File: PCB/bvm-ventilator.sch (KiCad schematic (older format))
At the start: 1 part, among them U13 IEC_CONNECTOR

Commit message: Checkpoint
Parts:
- added TP?: TestPoint, symbol Connector:TestPoint
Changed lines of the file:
@@
 $EndSheet
 $Sheet
-S 7200 4850 550  200
+S 6800 4850 550  200
 U 5E8EB699
 F0 "Alarm buzzer" 50
 F1 "BUZZER.sch" 50
-F2 "ENABLE" I R 7750 4950 50
-$EndSheet
-$Sheet
-S 7200 5300 550  600
+F2 "ENABLE" I R 7350 4950 50
+$EndSheet
+$Sheet
+S 6800 5300 550  600
 U 5E8F3A13
 F0 "OLED" 50
 F1 "SSD1306_OLED.sch" 50
-F2 "SCL" I R 7750 5500 50
-F3 "SDA" I R 7750 5400 50
-F4 "MOSI" I L 7200 5400 50
-F5 "SCK" I L 7200 5500 50
-F6 "DC" I L 7200 5700 50
-F7 "CS" I L 7200 5800 50
-F8 "RES" I L 7200 5600 50
+F2 "SCL" I R 7350 5500 50
+F3 "SDA" I R 7350 5400 50
+F4 "MOSI" I L 6800 5400 50
+F5 "SCK" I L 6800 5500 50
+F6 "DC" I L 6800 5700 50
+F7 "CS" I L 6800 5800 50
+F8 "RES" I L 6800 5600 50
 $EndSheet
 $Sheet
@@
 Text Label 6450 3900 2    50   ~ 0
 SCL
-Text Label 7750 5400 0    50   ~ 0
-SDA
-Text Label 7750 5500 0    50   ~ 0
+Text Label 7350 5400 0    50   ~ 0
+SDA
+Text Label 7350 5500 0    50   ~ 0
 SCL
 Text Label 3400 2800 0    50   ~ 0
@@
 Text Label 7300 3950 0    50   ~ 0
 STEPPER_DIR
-Text Label 7750 4950 0    50   ~ 0
+Text Label 7350 4950 0    50   ~ 0
 BUZZ_ENABLE
 Text Label 6450 3150 2    50   ~ 0
@@
 VBATT_SENSE
 $Sheet
-S 5450 4850 550  400
+S 5050 4850 550  400
 U 5E8BEE14
 F0 "Rotarty Encoder" 50
 F1 "ROTARY_ENCODER.sch" 50
-F2 "A" O R 6000 4950 50
-F3 "B" O R 6000 5050 50
-F4 "BUTTON" O R 6000 5150 50
-$EndSheet
-Text Label 6000 4950 0    50   ~ 0
+F2 "A" O R 5600 4950 50
+F3 "B" O R 5600 5050 50
+F4 "BUTTON" O R 5600 5150 50
+$EndSheet
+Text Label 5600 4950 0    50   ~ 0
 ROTARY_ENCODER_A
-Text Label 6000 5050 0    50   ~ 0
+Text Label 5600 5050 0    50   ~ 0
 ROTARY_ENCODER_B
-Text Label 6000 5150 0    50   ~ 0
+Text Label 5600 5150 0    50   ~ 0
 ROTARY_ENCODER_BUTTON
 Text Label 7300 3350 0    50   ~ 0
@@
 ROTARY_ENCODER_BUTTON
 $Sheet
-S 5450 5500 550  200
+S 5050 5500 550  200
 U 5E8CBD7F
 F0 "BUTTON_1" 50
 F1 "BUTTON.sch" 50
-F2 "OUT" O R 6000 5600 50
-$EndSheet
-Text Label 6000 5600 0    50   ~ 0
+F2 "OUT" O R 5600 5600 50
+$EndSheet
+Text Label 5600 5600 0    50   ~ 0
 BUTTON_1
 Text Label 6450 3450 2    50   ~ 0
@@
 Text Label 6450 3550 2    50   ~ 0
 DISPLAY_DC
-Text Label 7200 5700 2    50   ~ 0
+Text Label 6800 5700 2    50   ~ 0
 DISPLAY_DC
-Text Label 7200 5800 2    50   ~ 0
+Text Label 6800 5800 2    50   ~ 0
 DISPLAY_CS
-Text Label 7200 5600 2    50   ~ 0
+Text Label 6800 5600 2    50   ~ 0
 MISO
-Text Label 7200 5400 2    50   ~ 0
+Text Label 6800 5400 2    50   ~ 0
 MOSI
-Text Label 7200 5500 2    50   ~ 0
+Text Label 6800 5500 2    50   ~ 0
 SCK
 Wire Notes Line
 	4950 4700 4950 6050
 Wire Notes Line
-	4950 6050 8350 6050
-Wire Notes Line
-	8350 6050 8350 4700
-Wire Notes Line
-	8350 4700 4950 4700
+	4950 6050 7900 6050
+Wire Notes Line
+	7900 6050 7900 4700
+Wire Notes Line
+	7900 4700 4950 4700
 Text Notes 2750 3850 0    79   ~ 0
 Motion Control
@@
 Text Notes 4550 2950 0    79   ~ 0
 Misc.
+$Comp
+L Connector:TestPoint TP?
+U 1 1 5E8ED4B0
+P 8500 5000
+F 0 "TP?" H 8558 5118 50  0000 L CNN
+F 1 "TestPoint" H 8558 5027 50  0000 L CNN
+F 2 "" H 8700 5000 50  0001 C CNN
+F 3 "~" H 8700 5000 50  0001 C CNN
+	1    8500 5000
+	1    0    0    -1
+$EndComp
 $EndSCHEMATC

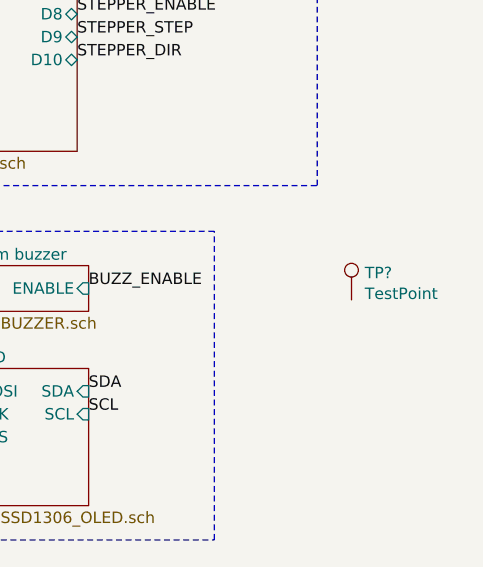
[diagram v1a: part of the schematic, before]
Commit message: Moved submodules into PCB subdirectory
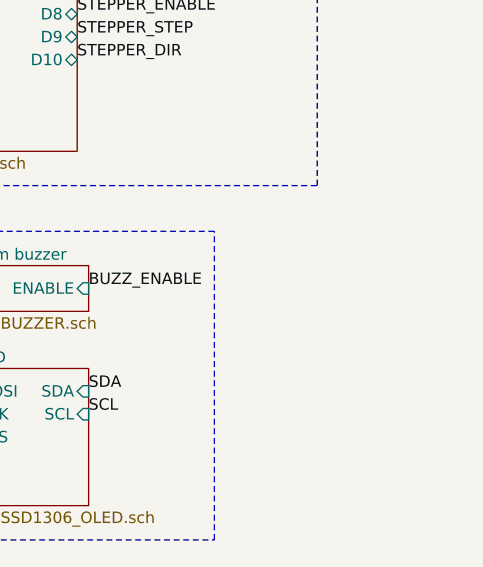
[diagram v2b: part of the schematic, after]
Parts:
- removed TP?: TestPoint, symbol Connector:TestPoint
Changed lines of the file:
@@
 Text Notes 4550 2950 0    79   ~ 0
 Misc.
-$Comp
-L Connector:TestPoint TP?
-U 1 1 5E8ED4B0
-P 8500 5000
-F 0 "TP?" H 8558 5118 50  0000 L CNN
-F 1 "TestPoint" H 8558 5027 50  0000 L CNN
-F 2 "" H 8700 5000 50  0001 C CNN
-F 3 "~" H 8700 5000 50  0001 C CNN
-	1    8500 5000
-	1    0    0    -1
-$EndComp
 $EndSCHEMATC

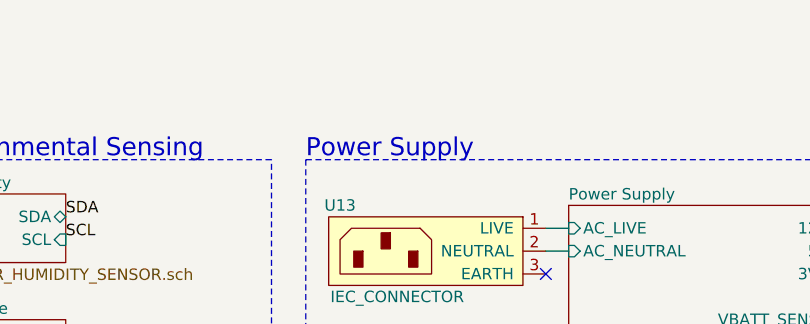
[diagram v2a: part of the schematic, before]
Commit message: Added test points to sensors
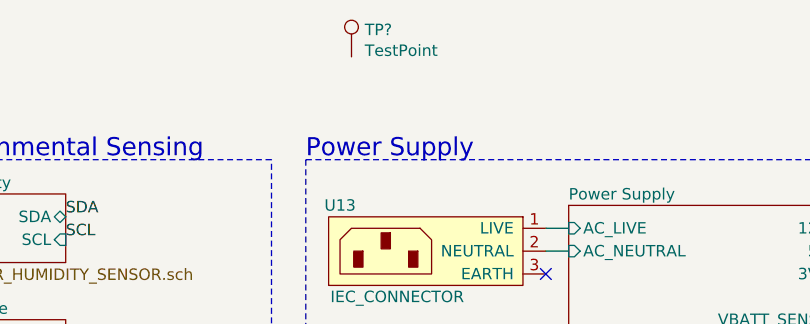
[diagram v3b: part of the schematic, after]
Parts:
- added TP?: TestPoint, symbol Connector:TestPoint
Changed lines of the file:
@@
 Text Notes 4550 2950 0    79   ~ 0
 Misc.
+$Comp
+L Connector:TestPoint TP?
+U 1 1 5E923993
+P 4650 1300
+F 0 "TP?" H 4708 1418 50  0000 L CNN
+F 1 "TestPoint" H 4708 1327 50  0000 L CNN
+F 2 "" H 4850 1300 50  0001 C CNN
+F 3 "~" H 4850 1300 50  0001 C CNN
+	1    4650 1300
+	1    0    0    -1
+$EndComp
 $EndSCHEMATC

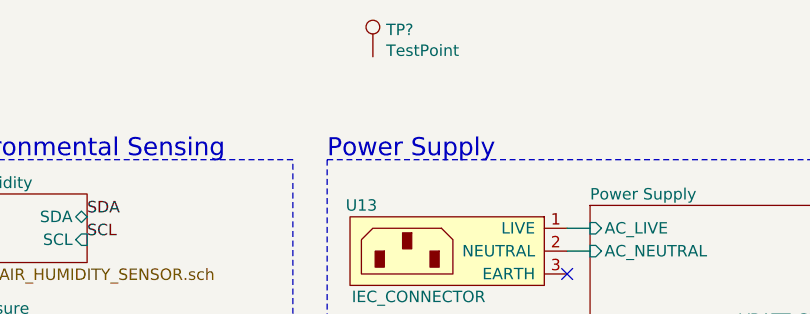
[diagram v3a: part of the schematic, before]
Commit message: Added correct DRV breakout and added testpoints
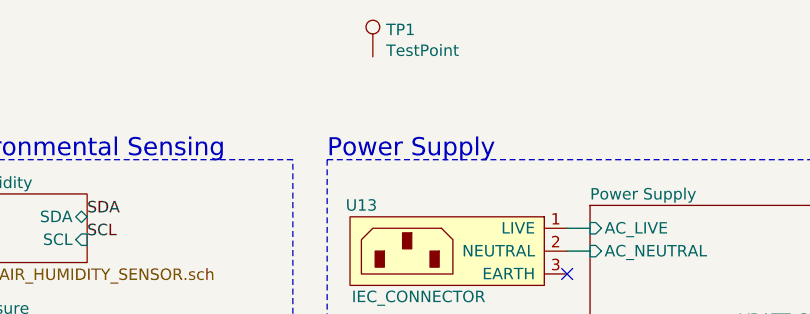
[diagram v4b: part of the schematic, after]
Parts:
- gave numbers to parts that had none: 1
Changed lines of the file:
@@
 Misc.
 $Comp
-L Connector:TestPoint TP?
+L Connector:TestPoint TP1
 U 1 1 5E923993
 P 4650 1300
-F 0 "TP?" H 4708 1418 50  0000 L CNN
+F 0 "TP1" H 4708 1418 50  0000 L CNN
 F 1 "TestPoint" H 4708 1327 50  0000 L CNN
 F 2 "" H 4850 1300 50  0001 C CNN

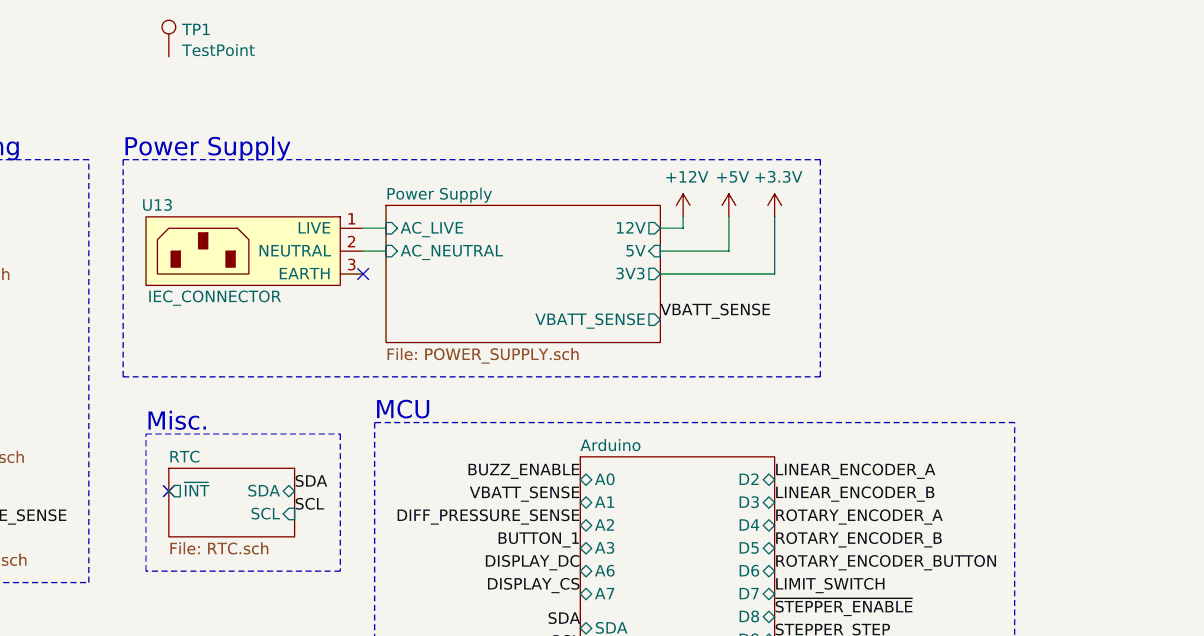
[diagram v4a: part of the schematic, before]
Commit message: Added test points to PSU
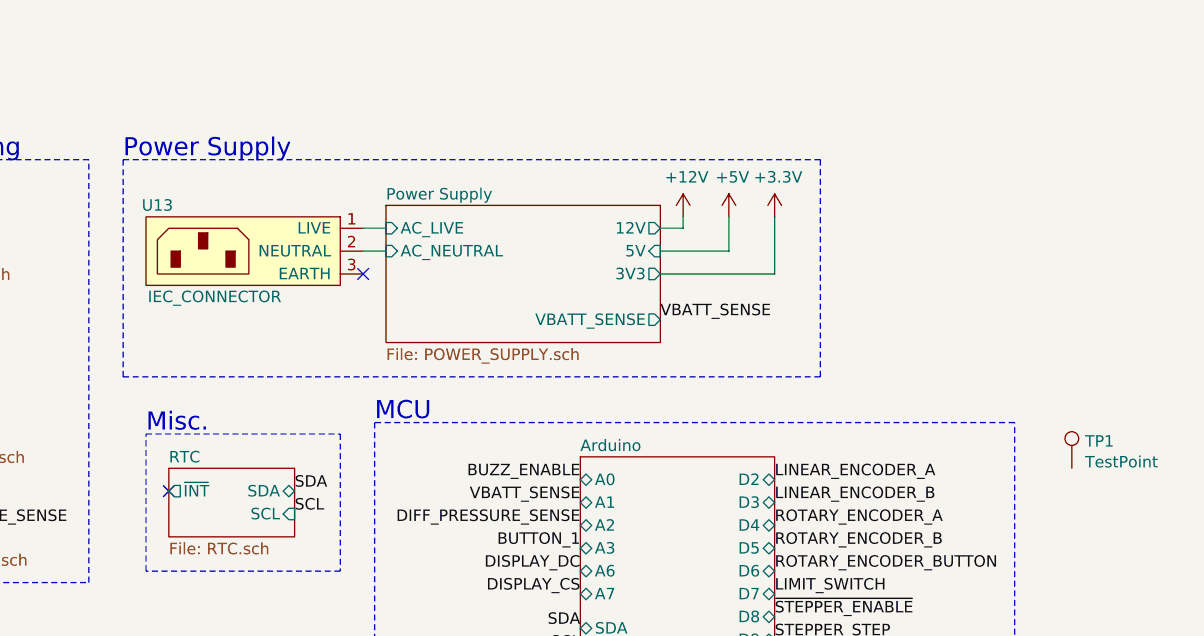
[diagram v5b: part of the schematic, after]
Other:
- moved on the sheet: TP1
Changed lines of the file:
@@
 L Connector:TestPoint TP1
 U 1 1 5E923993
-P 4650 1300
-F 0 "TP1" H 4708 1418 50  0000 L CNN
-F 1 "TestPoint" H 4708 1327 50  0000 L CNN
-F 2 "" H 4850 1300 50  0001 C CNN
-F 3 "~" H 4850 1300 50  0001 C CNN
-	1    4650 1300
+P 8600 3100
+F 0 "TP1" H 8658 3218 50  0000 L CNN
+F 1 "TestPoint" H 8658 3127 50  0000 L CNN
+F 2 "" H 8800 3100 50  0001 C CNN
+F 3 "~" H 8800 3100 50  0001 C CNN
+	1    8600 3100
 	1    0    0    -1
 $EndComp

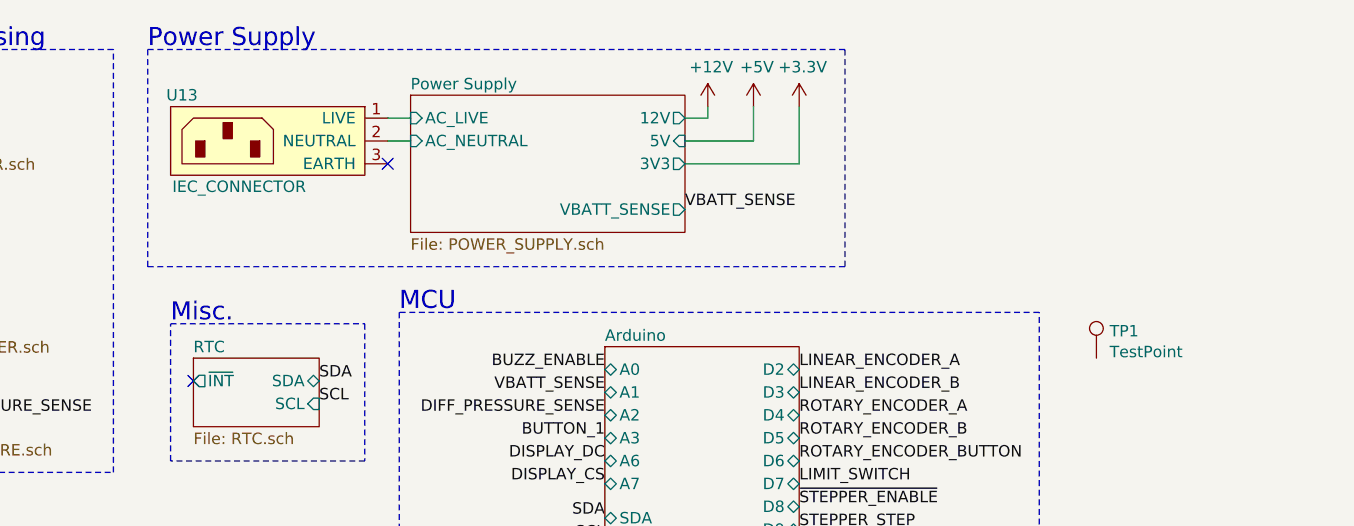
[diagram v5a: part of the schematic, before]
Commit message: Added remaining test points
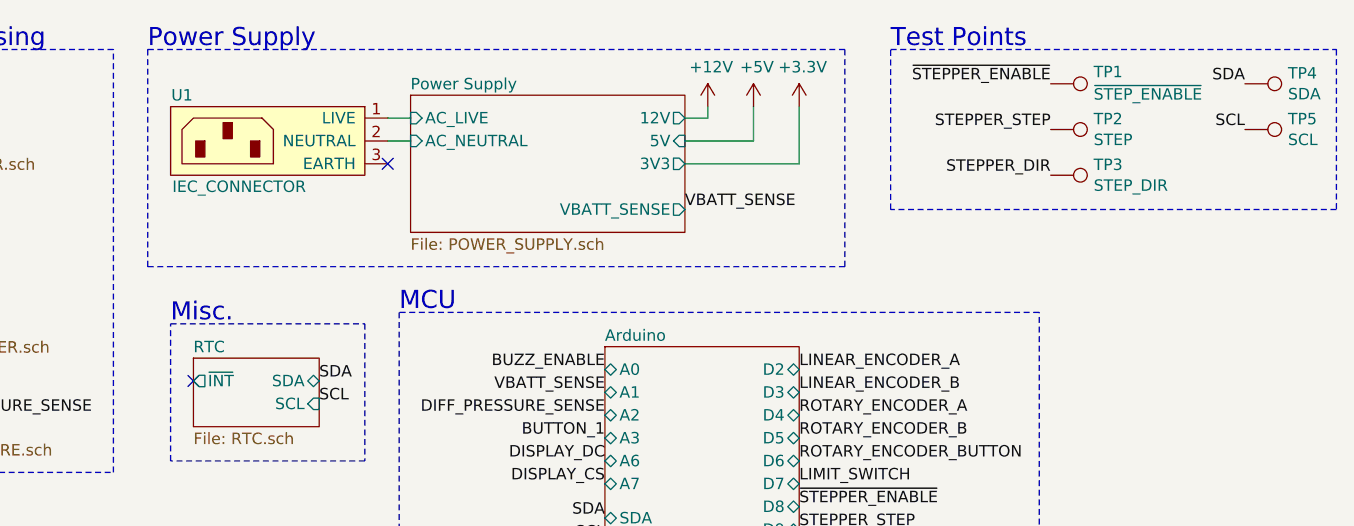
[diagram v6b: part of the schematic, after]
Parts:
- added TP2: STEP, symbol Connector:TestPoint
- added TP3: STEP_DIR, symbol Connector:TestPoint
- added TP4: SDA, symbol Connector:TestPoint
- added TP5: SCL, symbol Connector:TestPoint
- TP1: value TestPoint -> ~STEP_ENABLE
- renumbered U13 to U1
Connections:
- net SCL: now also TP5.1
- net SDA: now also TP4.1
- net STEPPER_DIR: now also TP3.1
- net STEPPER_STEP: now also TP2.1
- net ~STEPPER_ENABLE: now also TP1.1
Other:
- note added: "Test Points"
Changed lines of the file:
@@
 VBATT_SENSE
 $Comp
-L power:+3.3V #PWR04
+L power:+3.3V #PWR05
 U 1 1 5E8B3135
 P 7300 2000
-F 0 "#PWR04" H 7300 1850 50  0001 C CNN
+F 0 "#PWR05" H 7300 1850 50  0001 C CNN
 F 1 "+3.3V" H 7315 2173 50  0000 C CNN
 F 2 "" H 7300 2000 50  0001 C CNN
@@
 SCL
 $Comp
-L power:+5V #PWR062
+L power:+5V #PWR04
 U 1 1 5E93ECEE
 P 7100 2000
-F 0 "#PWR062" H 7100 1850 50  0001 C CNN
+F 0 "#PWR04" H 7100 1850 50  0001 C CNN
 F 1 "+5V" H 7115 2173 50  0000 C CNN
 F 2 "" H 7100 2000 50  0001 C CNN
@@
 NoConn ~ 5500 2250
 $Comp
-L custom:IEC_CONNECTOR U13
+L custom:IEC_CONNECTOR U1
 U 1 1 5E9816BB
 P 5000 2150
-F 0 "U13" H 5400 2350 50  0000 C CNN
+F 0 "U1" H 5400 2350 50  0000 C CNN
 F 1 "IEC_CONNECTOR" H 5150 1950 50  0000 C CNN
 F 2 "" H 5200 2100 50  0001 C CNN
@@
 Text Notes 4550 2950 0    79   ~ 0
 Misc.
+Text Label 9250 1900 2    50   ~ 0
+SDA
+Text Label 9250 2100 2    50   ~ 0
+SCL
+Text Label 8400 2100 2    50   ~ 0
+STEPPER_STEP
+Text Label 8400 2300 2    50   ~ 0
+STEPPER_DIR
+Text Label 8400 1900 2    50   ~ 0
+~STEPPER_ENABLE
 $Comp
 L Connector:TestPoint TP1
-U 1 1 5E923993
-P 8600 3100
-F 0 "TP1" H 8658 3218 50  0000 L CNN
-F 1 "TestPoint" H 8658 3127 50  0000 L CNN
-F 2 "" H 8800 3100 50  0001 C CNN
-F 3 "~" H 8800 3100 50  0001 C CNN
-	1    8600 3100
-	1    0    0    -1
-$EndComp
+U 1 1 5E9B874A
+P 8400 1900
+F 0 "TP1" V 8348 2088 50  0000 L CNN
+F 1 "~STEP_ENABLE" V 8446 2088 50  0000 L CNN
+F 2 "" H 8600 1900 50  0001 C CNN
+F 3 "~" H 8600 1900 50  0001 C CNN
+	1    8400 1900
+	0    1    1    0
+$EndComp
+$Comp
+L Connector:TestPoint TP2
+U 1 1 5E9B88D9
+P 8400 2100
+F 0 "TP2" V 8354 2288 50  0000 L CNN
+F 1 "STEP" V 8445 2288 50  0000 L CNN
+F 2 "" H 8600 2100 50  0001 C CNN
+F 3 "~" H 8600 2100 50  0001 C CNN
+	1    8400 2100
+	0    1    1    0
+$EndComp
+$Comp
+L Connector:TestPoint TP3
+U 1 1 5E9B8AC5
+P 8400 2300
+F 0 "TP3" V 8354 2488 50  0000 L CNN
+F 1 "STEP_DIR" V 8445 2488 50  0000 L CNN
+F 2 "" H 8600 2300 50  0001 C CNN
+F 3 "~" H 8600 2300 50  0001 C CNN
+	1    8400 2300
+	0    1    1    0
+$EndComp
+$Comp
+L Connector:TestPoint TP4
+U 1 1 5E9BDEC3
+P 9250 1900
+F 0 "TP4" V 9204 2088 50  0000 L CNN
+F 1 "SDA" V 9295 2088 50  0000 L CNN
+F 2 "" H 9450 1900 50  0001 C CNN
+F 3 "~" H 9450 1900 50  0001 C CNN
+	1    9250 1900
+	0    1    1    0
+$EndComp
+$Comp
+L Connector:TestPoint TP5
+U 1 1 5E9BE027
+P 9250 2100
+F 0 "TP5" V 9204 2288 50  0000 L CNN
+F 1 "SCL" V 9295 2288 50  0000 L CNN
+F 2 "" H 9450 2100 50  0001 C CNN
+F 3 "~" H 9450 2100 50  0001 C CNN
+	1    9250 2100
+	0    1    1    0
+$EndComp
+Wire Notes Line
+	7700 1750 9650 1750
+Wire Notes Line
+	9650 1750 9650 2450
+Wire Notes Line
+	9650 2450 7700 2450
+Wire Notes Line
+	7700 2450 7700 1750
+Text Notes 7700 1750 0    79   ~ 0
+Test Points
 $EndSCHEMATC

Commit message: Added majority footprints
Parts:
- TP1, TP2, TP3, TP4, TP5: footprint (none) -> custom:TestPoint_Pad_D1.5mm
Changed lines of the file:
@@
 F 0 "TP1" V 8348 2088 50  0000 L CNN
 F 1 "~STEP_ENABLE" V 8446 2088 50  0000 L CNN
-F 2 "" H 8600 1900 50  0001 C CNN
+F 2 "custom:TestPoint_Pad_D1.5mm" H 8600 1900 50  0001 C CNN
 F 3 "~" H 8600 1900 50  0001 C CNN
 	1    8400 1900
@@
 F 0 "TP2" V 8354 2288 50  0000 L CNN
 F 1 "STEP" V 8445 2288 50  0000 L CNN
-F 2 "" H 8600 2100 50  0001 C CNN
+F 2 "custom:TestPoint_Pad_D1.5mm" H 8600 2100 50  0001 C CNN
 F 3 "~" H 8600 2100 50  0001 C CNN
 	1    8400 2100
@@
 F 0 "TP3" V 8354 2488 50  0000 L CNN
 F 1 "STEP_DIR" V 8445 2488 50  0000 L CNN
-F 2 "" H 8600 2300 50  0001 C CNN
+F 2 "custom:TestPoint_Pad_D1.5mm" H 8600 2300 50  0001 C CNN
 F 3 "~" H 8600 2300 50  0001 C CNN
 	1    8400 2300
@@
 F 0 "TP4" V 9204 2088 50  0000 L CNN
 F 1 "SDA" V 9295 2088 50  0000 L CNN
-F 2 "" H 9450 1900 50  0001 C CNN
+F 2 "custom:TestPoint_Pad_D1.5mm" H 9450 1900 50  0001 C CNN
 F 3 "~" H 9450 1900 50  0001 C CNN
 	1    9250 1900
@@
 F 0 "TP5" V 9204 2288 50  0000 L CNN
 F 1 "SCL" V 9295 2288 50  0000 L CNN
-F 2 "" H 9450 2100 50  0001 C CNN
+F 2 "custom:TestPoint_Pad_D1.5mm" H 9450 2100 50  0001 C CNN
 F 3 "~" H 9450 2100 50  0001 C CNN
 	1    9250 2100

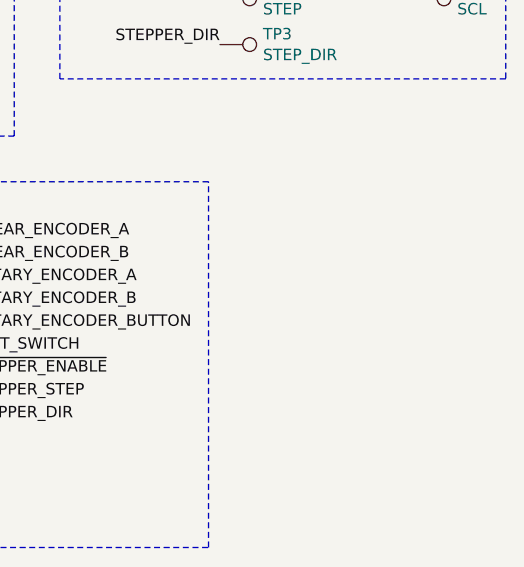
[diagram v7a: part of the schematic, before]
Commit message: Replaced Tant Caps with Alu
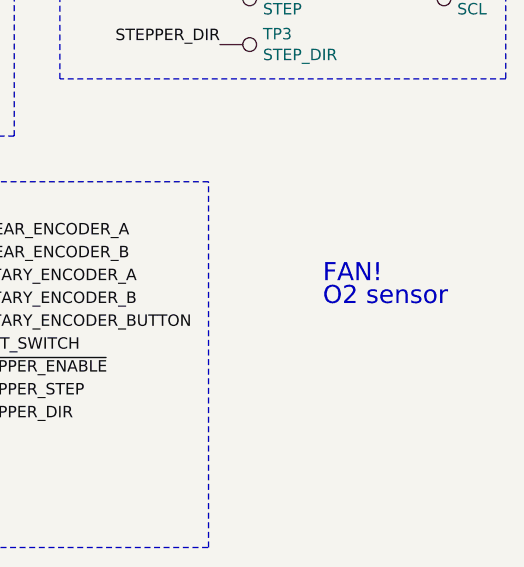
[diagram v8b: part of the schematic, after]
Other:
- note added: "FAN!"
- note added: "O2 sensor"
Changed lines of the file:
@@
 Text Notes 7700 1750 0    79   ~ 0
 Test Points
+Text Notes 8850 3350 0    79   ~ 0
+FAN!
+Text Notes 8850 3450 0    79   ~ 0
+O2 sensor
 $EndSCHEMATC
